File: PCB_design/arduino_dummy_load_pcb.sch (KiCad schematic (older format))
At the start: 109 parts, among them J1 Barrel_Jack, J2 Conn_02x08_Odd_Even, M1 REG, U1 LM324, U2 LM324

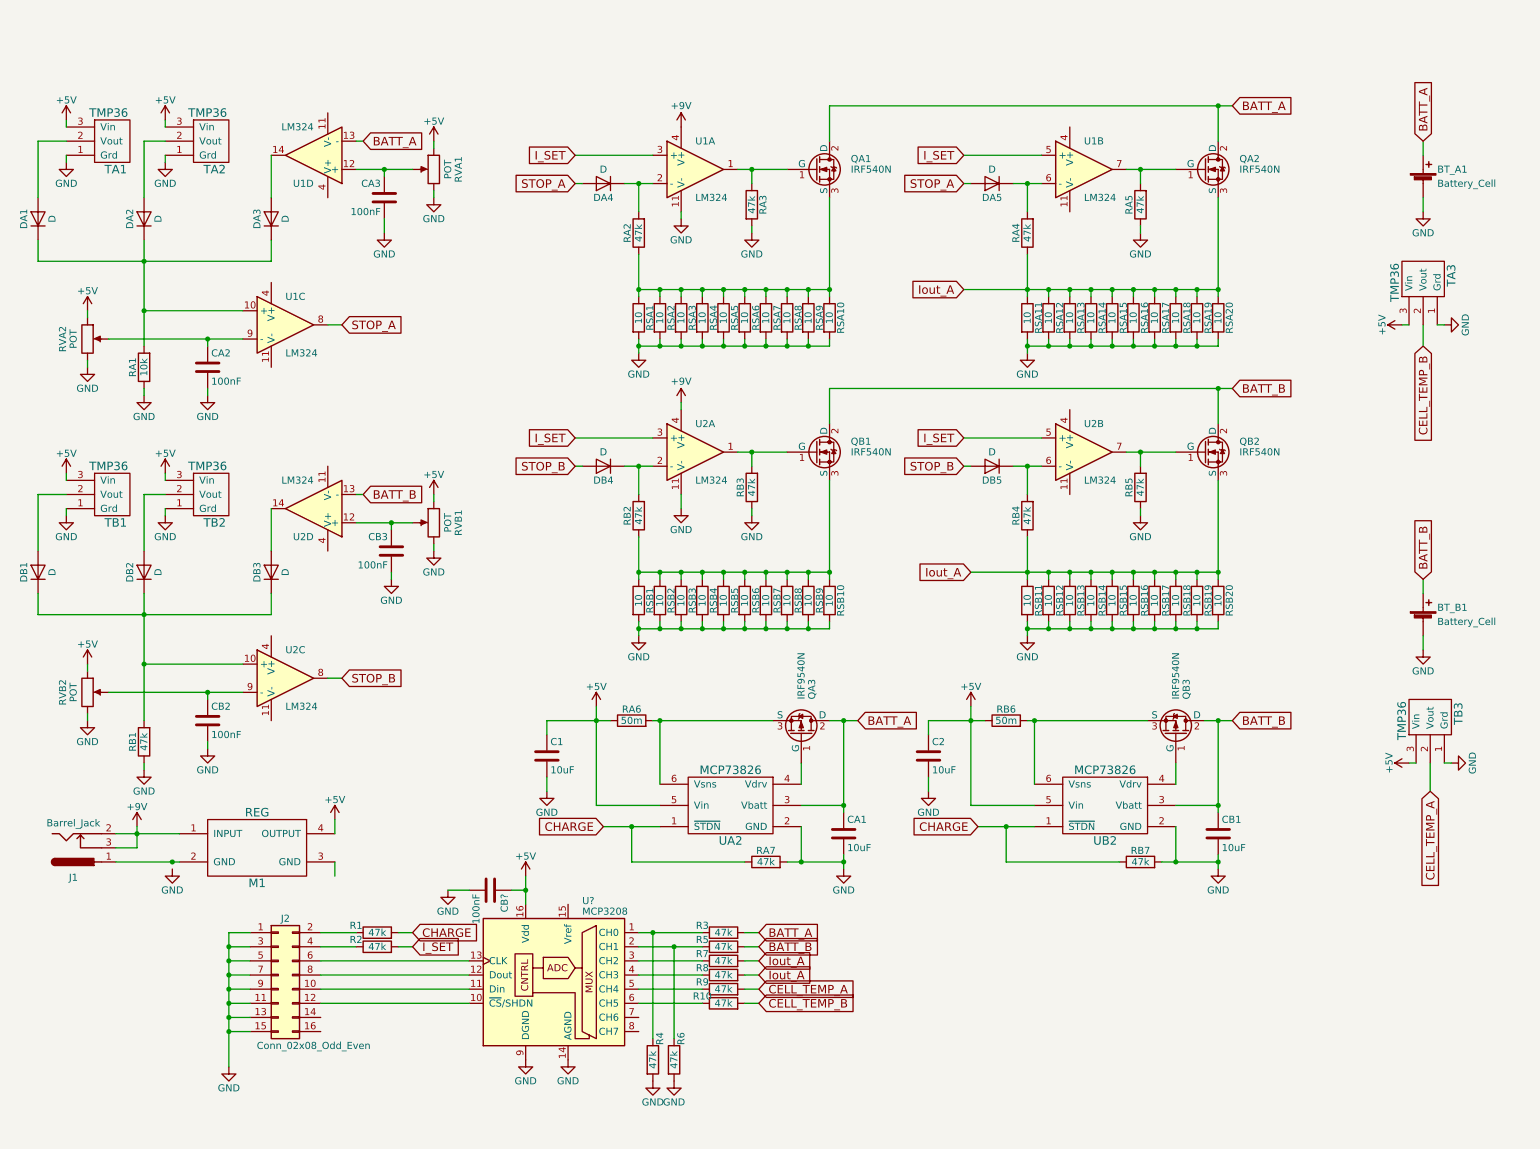
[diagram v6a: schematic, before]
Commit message: Fixed a few mistakes, Implemented reverse polarity protection w/ MOSFETs.
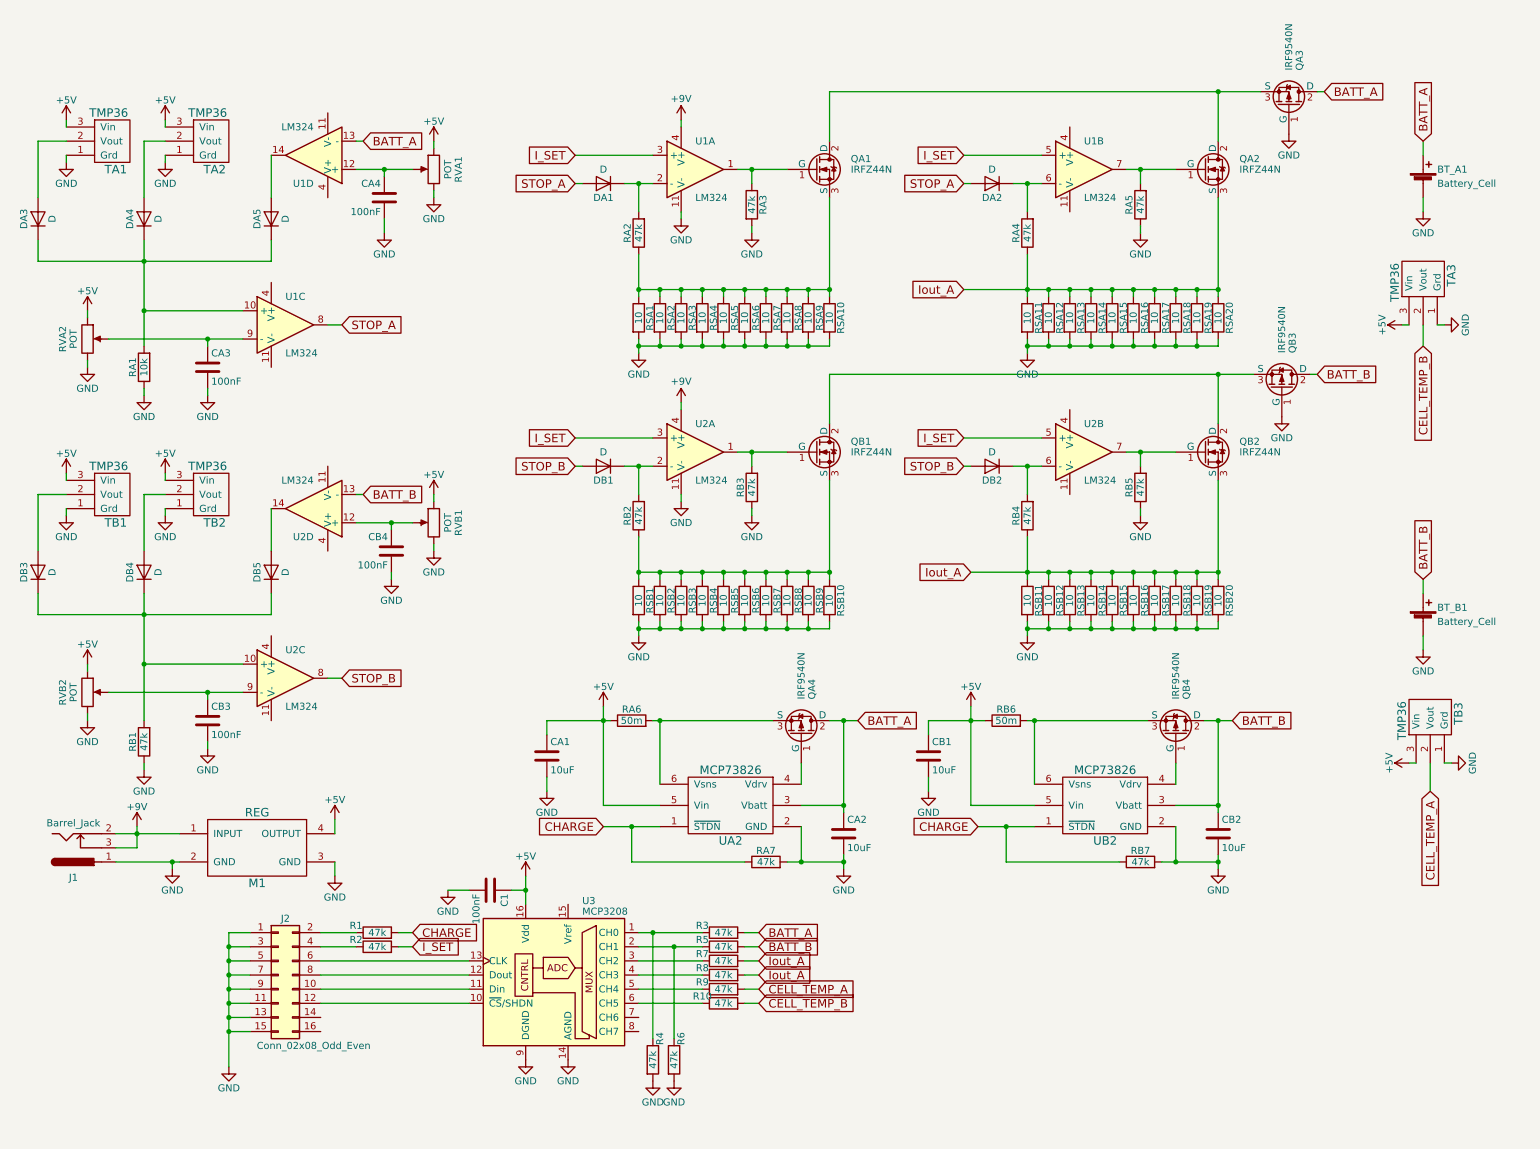
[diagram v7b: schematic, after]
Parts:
- removed DA4, DA5: D, Diodes_SMD:D_SOD-123, symbol D
- added DA1, DA2: D, Diodes_SMD:D_SOD-123, symbol D
- added QA3, QB3: IRF9540N, TO_SOT_Packages_THT:TO-220-3_Vertical, symbol IRF9540N
- QA1, QA2, QB1, QB2: value IRF540N -> IRFZ44N
- gave numbers to parts that had none: 2
- renumbered C1 to CA1, CA1 to CA2, CA2 to CA3, CA3 to CA4, C2 to CB1, CB1 to CB2, CB2 to CB3, CB3 to CB4, DA1 to DA3, DA2 to DA4, DA3 to DA5, DB4 to DB1, DB5 to DB2, DB1 to DB3, DB2 to DB4, DB3 to DB5, QA3 to QA4, QB3 to QB4
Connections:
- net BATT_A: now also QA3.2 (D); no longer QA1.2 (D), QA2.2 (D)
- net BATT_B: now also QB3.2 (D); no longer QB1.2 (D), QB2.2 (D)
- net GND: now also J1.1, M1.2 (GND), M1.3 (GND), QA3.1 (G), QB3.1 (G)
- net STOP_A: now also DA1.2 (A), DA2.2 (A)
- net at RA4.2, U1.6 (-): now also DA2.1 (K)
- net at RA2.2, U1.2 (-): now also DA1.1 (K)
- new net: QA1.2 (D), QA2.2 (D), QA3.3 (S)
- new net: QB1.2 (D), QB2.2 (D), QB3.3 (S)

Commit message: refactored the redundant battery testing units into hierarchical blocks. TODO: still need to add voltage reference component and create custom PCB footprint for the battery.
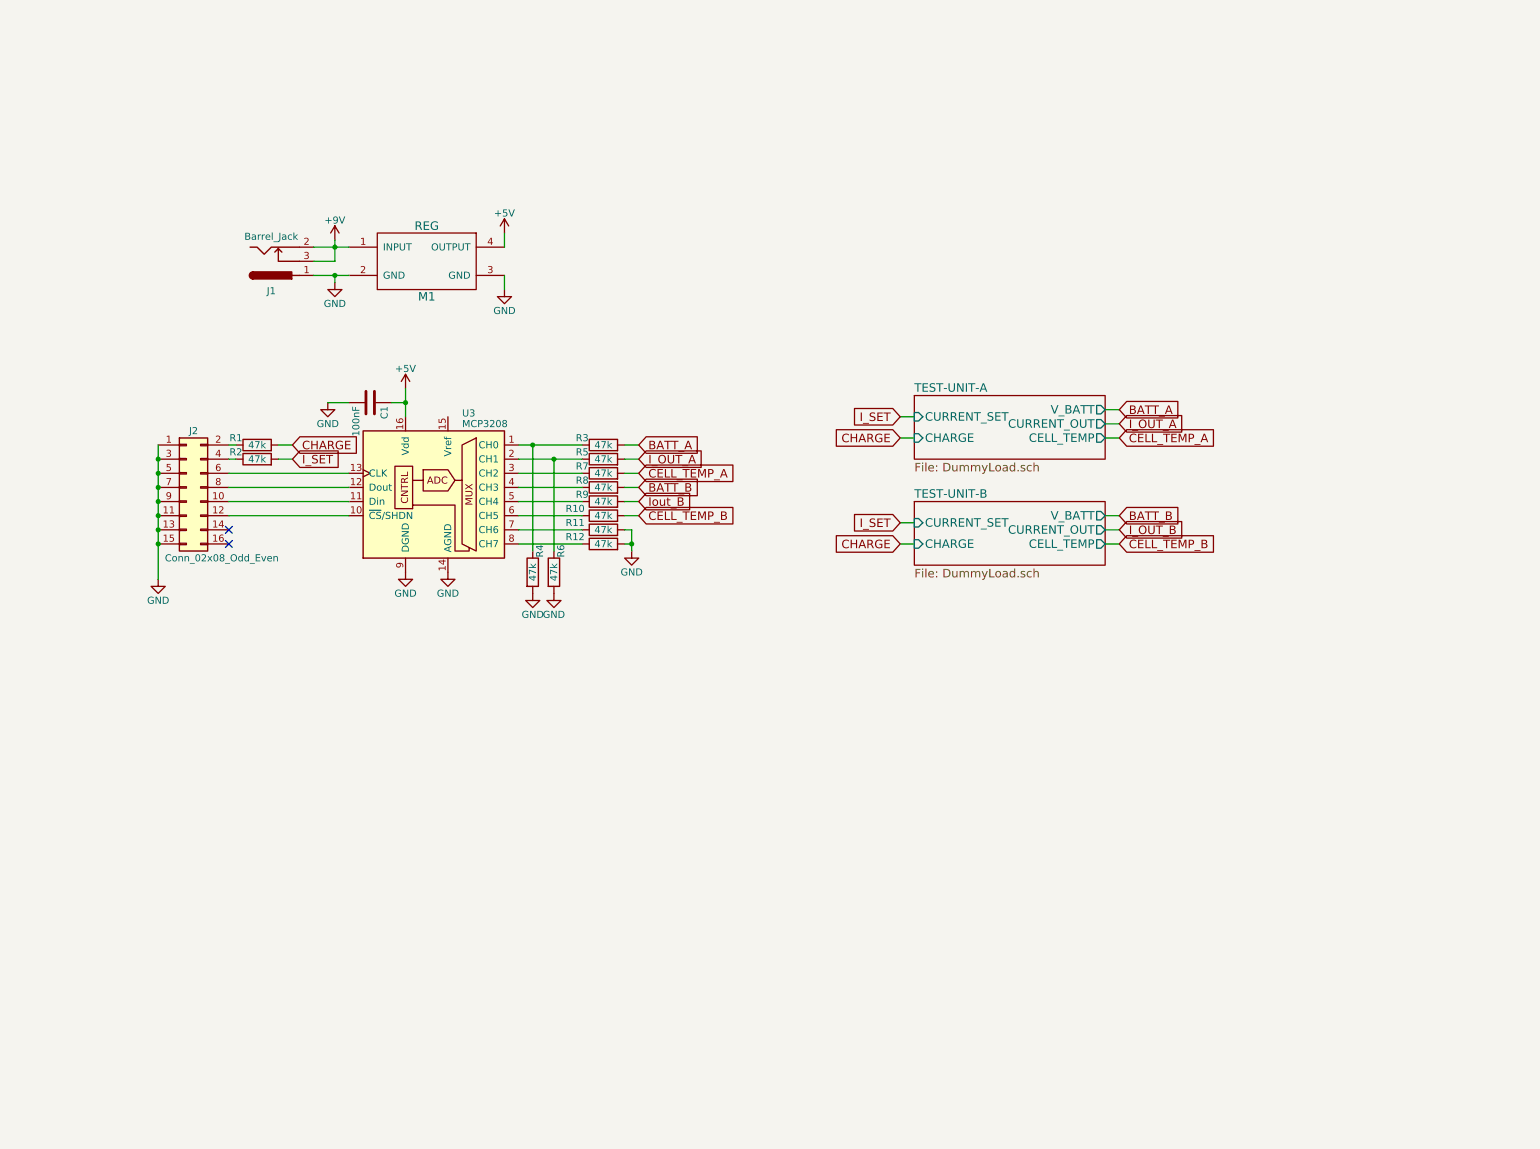
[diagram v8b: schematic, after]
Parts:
- removed BT_A1, BT_B1: Battery_Cell, symbol Battery_Cell
- removed CA1, CA2, CB1, CB2: 10uF, Capacitors_SMD:C_0805_HandSoldering, symbol C
- removed CA3, CA4, CB3, CB4: 100nF, Capacitors_SMD:C_0805_HandSoldering, symbol C
- removed DA1, DA2, DA3, DA4, DA5, DB1, DB2, DB3, DB4, DB5: D, Diodes_SMD:D_SOD-123, symbol D
- removed QA1, QA2, QB1, QB2: IRFZ44N, TO_SOT_Packages_THT:TO-220-3_Vertical, symbol IRF540N
- removed QA3, QA4, QB3, QB4: IRF9540N, TO_SOT_Packages_THT:TO-220-3_Vertical, symbol IRF9540N
- removed RA1: 10k, Resistors_SMD:R_0805_HandSoldering, symbol R
- removed RA2, RA3, RA4, RA5, RA7, RB1, RB2, RB3, RB4, RB5, RB7: 47k, Resistors_SMD:R_0805_HandSoldering, symbol R
- removed RA6, RB6: 50m, Resistors_SMD:R_2512_HandSoldering, symbol R
- removed RSA1, RSA10, RSA11, RSA12, RSA13, RSA14, RSA15, RSA16, RSA17, RSA18, RSA19, RSA2, RSA20, RSA3, RSA4, RSA5, RSA6, RSA7, RSA8, RSA9, RSB1, RSB10, RSB11, RSB12, RSB13, RSB14, RSB15, RSB16, RSB17, RSB18, RSB19, RSB2, RSB20, RSB3, RSB4, RSB5, RSB6, RSB7, RSB8, RSB9: 10, Resistors_THT:R_Axial_DIN0617_L17.0mm_D6.0mm_P7.62mm_Vertical, symbol R
- removed RVA1, RVA2, RVB1, RVB2: POT, Potentiometers:Potentiometer_Trimmer_ACP_CA6v_Horizontal_MountLS, symbol POT
- removed TA1, TA2, TA3, TB1, TB2, TB3: TMP36, TO_SOT_Packages_THT:TO-92_Inline_Wide, symbol TMP36
- removed U1, U2: LM324, Housings_SOIC:SOIC-14_3.9x8.7mm_Pitch1.27mm, symbol LM324
- removed UA2, UB2: MCP73826, TO_SOT_Packages_SMD:SOT-23-6_Handsoldering, symbol MCP73826
- added R11, R12: 47k, Resistors_SMD:R_0805_HandSoldering, symbol R
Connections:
- net BATT_B: now also R8.2; no longer R5.2
- net CELL_TEMP_A: now also R7.2; no longer R9.2
- net GND: now also R11.2, R12.2
- net at U3.7 (CH6): now also R11.1
- net at U3.8 (CH7): now also R12.1
- removed net Iout_A: R7.2, R8.2
- new net I_OUT_A: R5.2
- new net Iout_B: R9.2
- no-connect marks 0 -> 2
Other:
- moved on the sheet: C1, J1, J2, M1, R1, R10, R2, R3, R4, R5, R6, R7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
